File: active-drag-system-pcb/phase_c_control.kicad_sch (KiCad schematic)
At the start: 18 parts, among them Q1 SIR182DP-T1-RE3, Q2 SIR182DP-T1-RE3, U11 IR2103, U12 INA180A3

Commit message: Add other two phases; remove CYW43 for scope reasons
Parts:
- renumbered C30 to C36, C31 to C37, C32 to C38, C33 to C39, C34 to C40, C35 to C41, D1 to D3, D2 to D4, Q1 to Q3, Q2 to Q4, R11 to R16, R10 to R17, R12 to R18, R13 to R19, R14 to R20, R15 to R21, U11 to U13, U12 to U14
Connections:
- net CURRENT_SENSE_A renamed CURRENT_SENSE_C
- net PHASE_A renamed PHASE_C
- net VOLTAGE_SENSE_A renamed VOLTAGE_SENSE_C

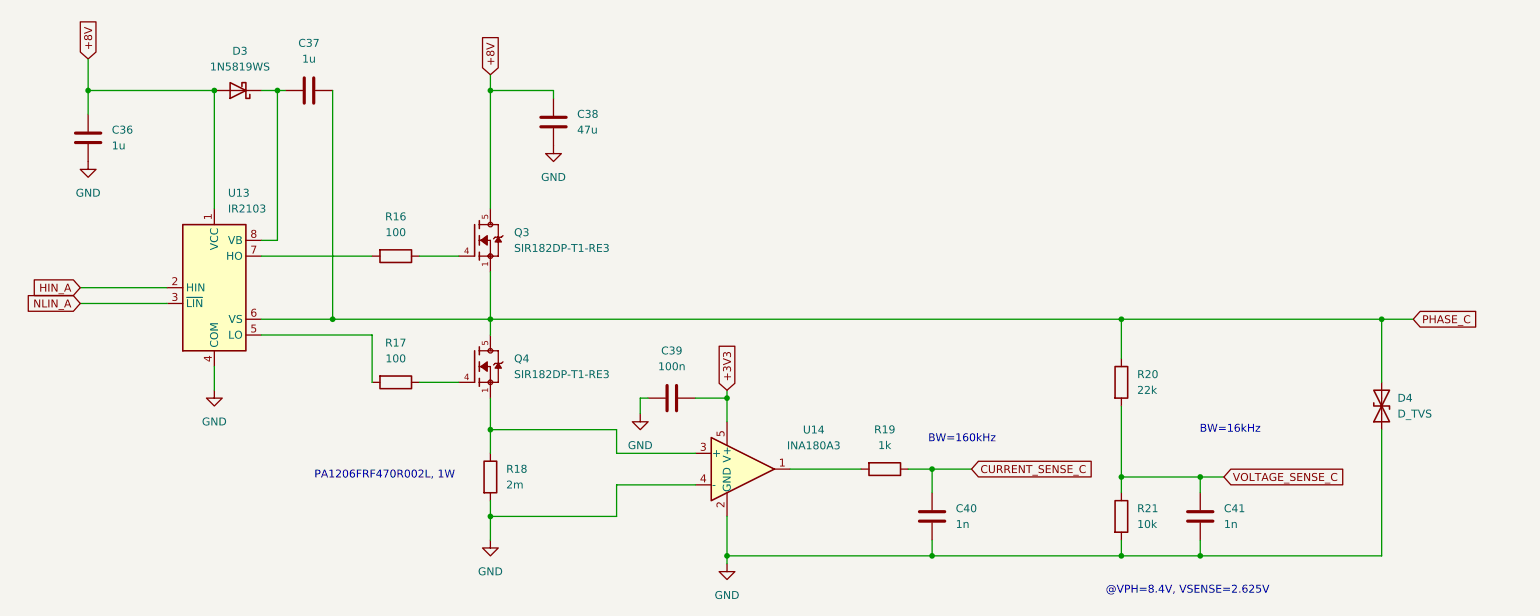
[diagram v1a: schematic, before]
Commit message: Swapped out regulators for higher current output; removed 8.4 V regulator; now two grounds (power and analog)
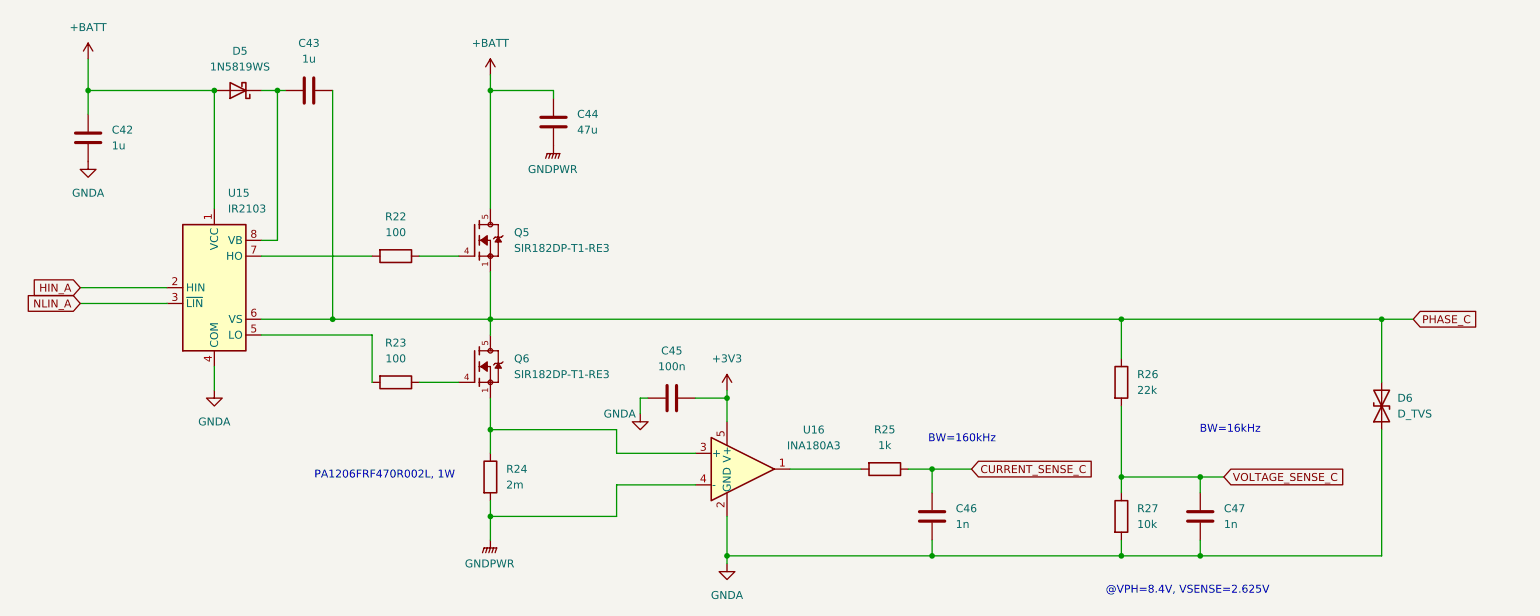
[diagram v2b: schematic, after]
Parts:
- renumbered C36 to C42, C37 to C43, C38 to C44, C39 to C45, C40 to C46, C41 to C47, D3 to D5, D4 to D6, Q3 to Q5, Q4 to Q6, R16 to R22, R17 to R23, R18 to R24, R19 to R25, R20 to R26, R21 to R27, U13 to U15, U14 to U16
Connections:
- net +8V renamed +BATT
- net GND renamed GNDA
- net GNDA: no longer C44.2, R24.2, U16.4 (-)
- new net GNDPWR: C44.2, R24.2, U16.4 (-)

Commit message: Literally everything has footprints and is pretty connected together on schematic except for IIM
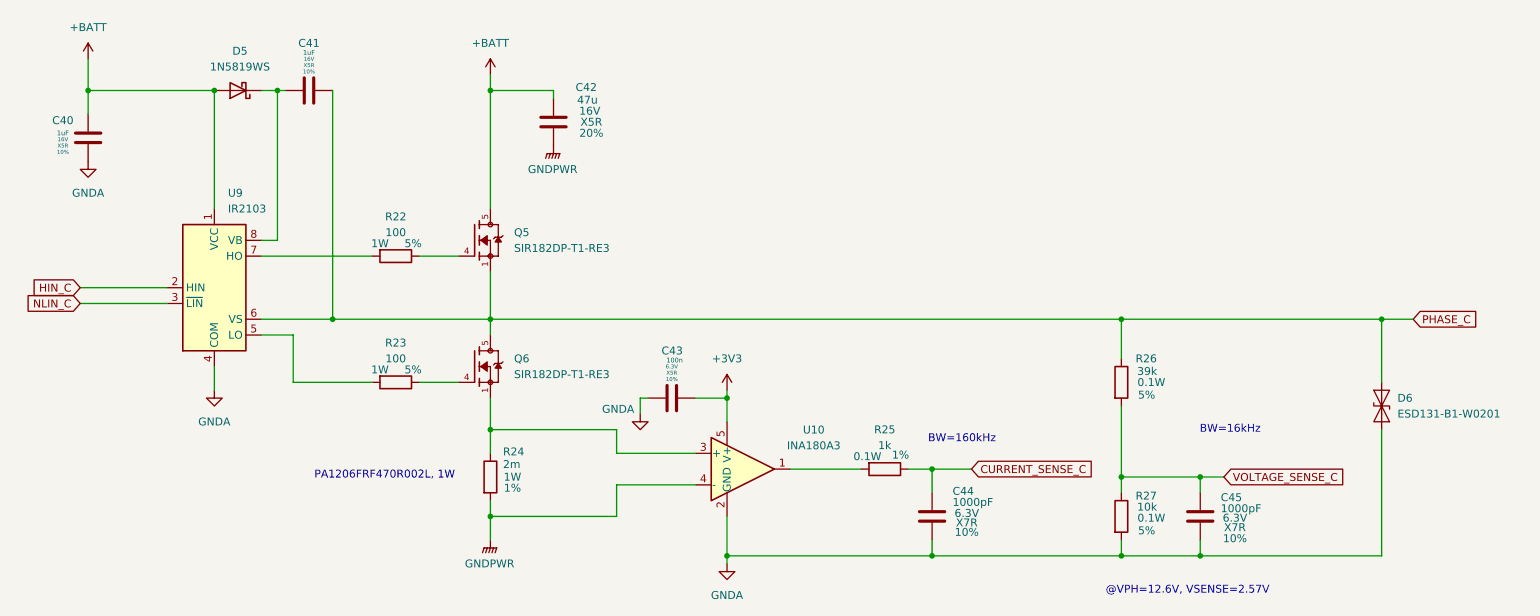
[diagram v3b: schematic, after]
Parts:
- removed C42: 1u, symbol Device:C
- removed C47: 1n, symbol Device:C
- removed D6: D_TVS, symbol Device:D_TVS
- added C40: 1uF, Capacitor_SMD:C_0402_1005Metric_Pad0.74x0.62mm_HandSolder, symbol Device:C
- added C43: 100n, Capacitor_SMD:C_0201_0603Metric_Pad0.64x0.40mm_HandSolder, symbol Device:C
- added D6: ESD131-B1-W0201, Diode_SMD:Infineon_SG-WLL-2-3_0.58x0.28_P0.36mm, symbol Diode:ESD131-B1-W0201
- C41: renamed from C43; value 1u -> 1uF; footprint (none) -> Capacitor_SMD:C_0402_1005Metric_Pad0.74x0.62mm_HandSolder; Dielectric (none) -> X5R; Max Voltage (none) -> 16V; Tolerance (none) -> 10%
- C42: renamed from C44; footprint (none) -> Capacitor_SMD:C_1210_3225Metric_Pad1.33x2.70mm_HandSolder; Dielectric (none) -> X5R; Max Voltage (none) -> 16V; Tolerance (none) -> 20%
- C44: renamed from C46; value 1n -> 1000pF; footprint (none) -> Capacitor_SMD:C_0402_1005Metric_Pad0.74x0.62mm_HandSolder; Dielectric (none) -> X7R; Max Voltage (none) -> 6.3V; Tolerance (none) -> 10%
- C45: value 100n -> 1000pF; footprint (none) -> Capacitor_SMD:C_0402_1005Metric_Pad0.74x0.62mm_HandSolder; Dielectric (none) -> X7R; Max Voltage (none) -> 6.3V; Tolerance (none) -> 10%
- R22, R23: footprint (none) -> Resistor_SMD:R_2512_6332Metric_Pad1.40x3.35mm_HandSolder; Power (none) -> 1W; Tolerance (none) -> 5%
- R24: footprint (none) -> Resistor_SMD:R_1206_3216Metric_Pad1.30x1.75mm_HandSolder; Power (none) -> 1W; Tolerance (none) -> 1%
- R25: footprint (none) -> Resistor_SMD:R_0402_1005Metric_Pad0.72x0.64mm_HandSolder; Power (none) -> 0.1W; Tolerance (none) -> 1%
- R26: value 22k -> 39k; footprint (none) -> Resistor_SMD:R_0402_1005Metric_Pad0.72x0.64mm_HandSolder; Power (none) -> 0.1W; Tolerance (none) -> 5%
- R27: footprint (none) -> Resistor_SMD:R_0402_1005Metric_Pad0.72x0.64mm_HandSolder; Power (none) -> 0.1W; Tolerance (none) -> 5%
- renumbered U16 to U10, U15 to U9
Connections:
- net +3V3: now also C43.2; no longer C45.1
- net +BATT: now also C40.1
- net GNDA: now also C40.2, C43.1, D6.1 (A1)
- net PHASE_C: now also D6.2 (A2)
- net VOLTAGE_SENSE_C: now also C45.1
- net HIN_A renamed HIN_C
- net NLIN_A renamed NLIN_C
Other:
- note added: "@VPH=12.6V, VSENSE=2.57V"
- note removed: "@VPH=8.4V, VSENSE=2.625V"

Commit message: Updated Footprint library; Started component placement for 5V regulator
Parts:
- Q5, Q6: footprint SIR182DP-T1-RE3:TRANS_SIR182DP-T1-RE3 -> ADS_Library:TRANS_SIR182DP-T1-RE3
- U9: value IR2103 -> IR2103STRPBF; footprint (none) -> ADS_Library:SO8N_INF-L
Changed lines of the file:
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@@
 			)
 		)
-		(property "Footprint" "SIR182DP-T1-RE3:TRANS_SIR182DP-T1-RE3"
+		(property "Footprint" "ADS_Library:TRANS_SIR182DP-T1-RE3"
 			(at 104.14 81.28 0)
 			(effects
@@
 			)
 		)
-		(property "Footprint" "SIR182DP-T1-RE3:TRANS_SIR182DP-T1-RE3"
+		(property "Footprint" "ADS_Library:TRANS_SIR182DP-T1-RE3"
 			(at 104.14 60.96 0)
 			(effects
@@
 			)
 		)
-		(property "Value" "IR2103"
+		(property "Value" "IR2103STRPBF"
 			(at 64.4241 55.88 0)
 			(effects
@@
 			)
 		)
-		(property "Footprint" ""
+		(property "Footprint" "ADS_Library:SO8N_INF-L"
 			(at 62.23 68.58 0)
 			(effects
